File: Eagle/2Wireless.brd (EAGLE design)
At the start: 62.7 x 31.8 mm, 22 parts, among them IC1 TCA9517A, IC2 VREGLD1117, IC3 MB85RS2MTAPNF-G-BDERE1, U1 PHOTON_WITH_HEADERS

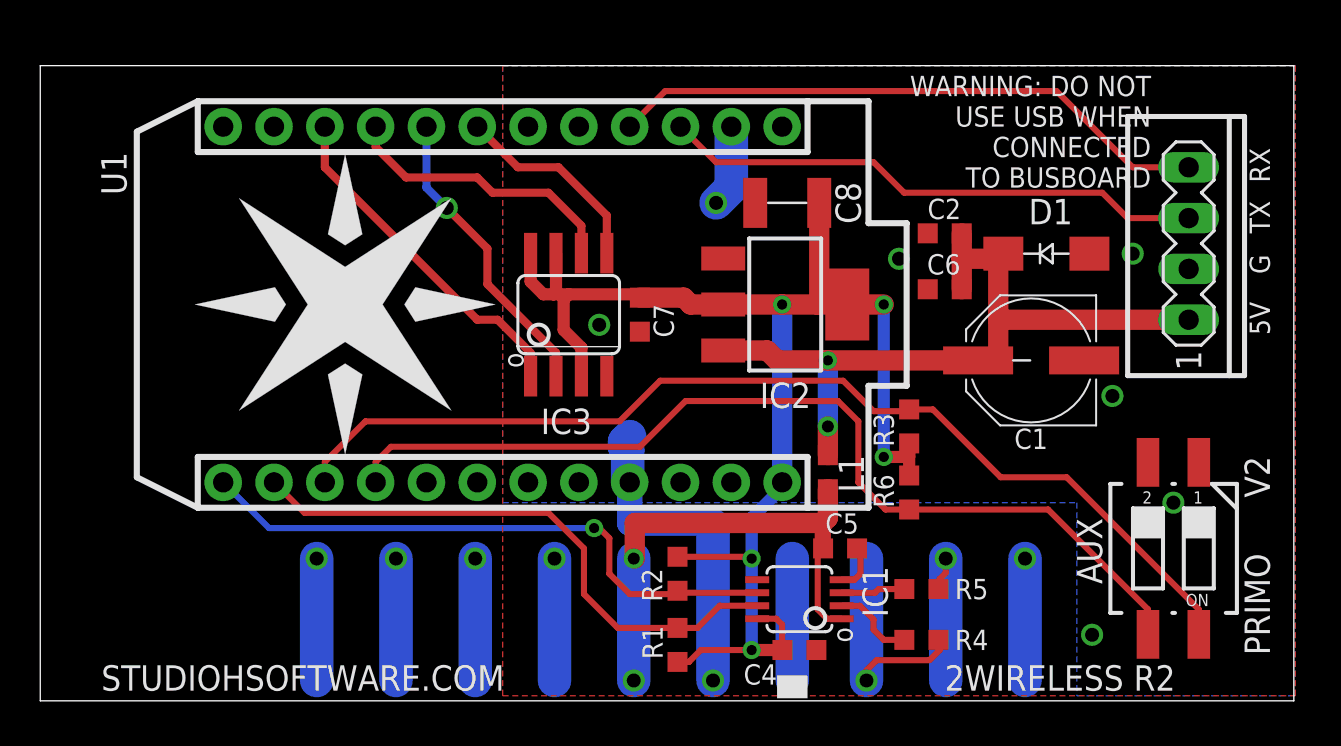
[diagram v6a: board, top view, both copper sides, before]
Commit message: Switch layout from Photon to Arduino MKR1000.
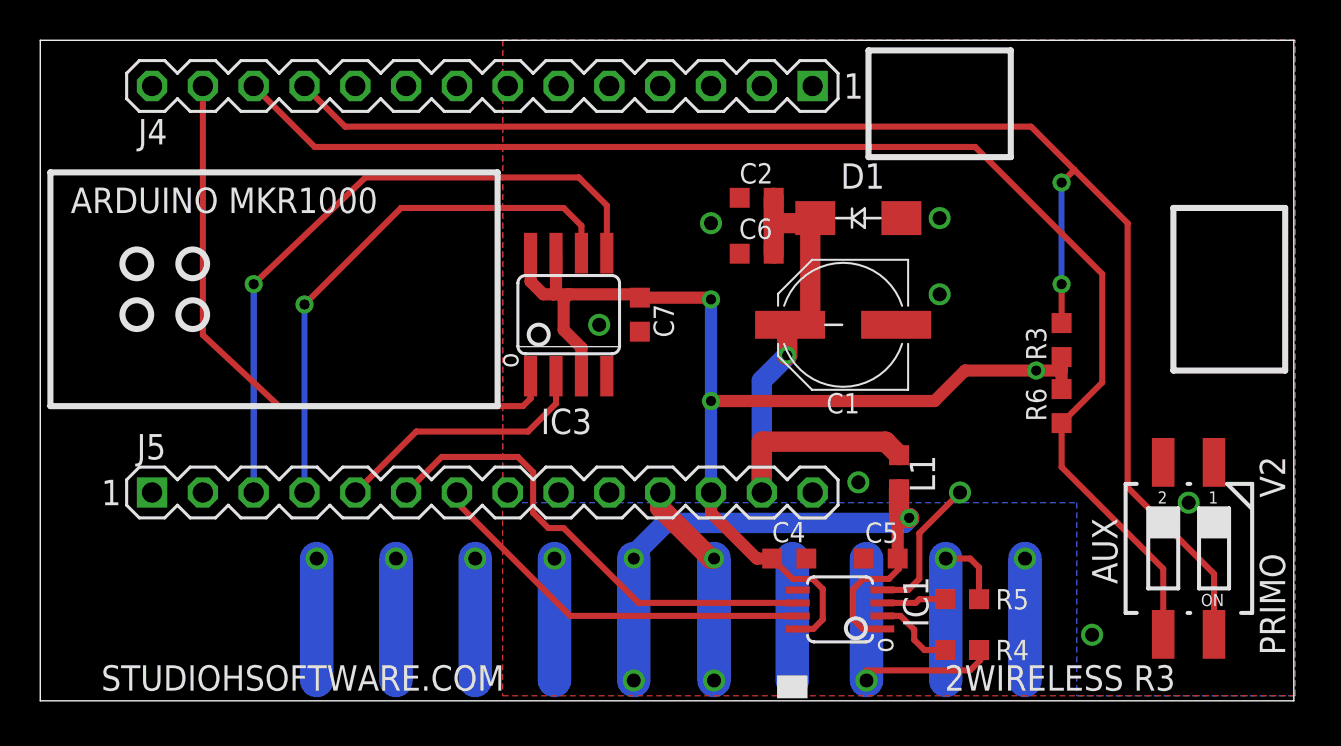
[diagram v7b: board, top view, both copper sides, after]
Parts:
- removed C8: 10u, studio_h:C1210
- removed IC2: VREGLD1117, studio_h:SOT223
- removed R1, R2: 2k, studio_h:R0603
- removed SV1: (no value), studio_h:MA04-1
- removed U$1: (no value), Particle:PARTICLE_LOGO_15MM
- removed U1: PHOTON_WITH_HEADERS, Particle:PHOTON
- added J4, J5: (no value), studio_h:MA14-1
- moved C1 9.56 mm to (40.1, 18.8)
- moved C2 9.56 mm to (35.8, 25.1)
- moved C6 9.56 mm to (35.8, 22.4)
- moved D1 9.56 mm to (40.9, 24.1)
- moved R3 8.76 mm to (51.1, 18.0)
- moved R6 8.76 mm to (51.1, 14.7)
- moved C4 4.60 mm to (37.4, 7.11)
- moved L1 3.56 mm to (42.9, 11.4)
- moved C5 2.09 mm to (42.0, 7.11), turned to 180 degrees
- moved R4 2.09 mm to (46.1, 2.54)
- moved R5 2.09 mm to (46.1, 5.08)
- moved IC1 2.09 mm to (40.0, 4.57)
- moved S1 0.76 mm to (57.4, 7.62)
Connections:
- removed net RX: SV1.4, U1.4
- removed net TX: SV1.3, U1.3
- removed net VBAT: U1.22
- removed net VIN: U1.1
- net !CS: now also J4.13; no longer U1.10
- net +5V: now also J5.13; no longer IC2.3, SV1.1
- net DGND: now also J5.11; no longer C8.2, IC2.1, SV1.2, U1.2, U1.21
- net DI-AUX: now also J4.12; no longer U1.16
- net DI-VERSION: now also J4.11; no longer U1.15
- net DPWR: now also J5.12; no longer C8.1, IC2.2, IC2.4, R1.2, R2.2, U1.24
- net MISO: now also J5.5; no longer U1.8
- net MOSI: now also J5.3; no longer U1.7
- net SCK: now also J5.4; no longer U1.9
- net SCL: now also J5.7; no longer R1.1, U1.14
- net SDA: now also J5.6; no longer R2.1, U1.13
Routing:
- net RX: track 30.3 -> 0.00 mm
- net TX: track 27.3 -> 0.00 mm
- net MOSI: track 10.2 -> 33.2 mm, vias 0 -> 1
- net DI-VERSION: track 52.4 -> 74.3 mm, vias 0 -> 2
- net DI-AUX: track 48.9 -> 67.3 mm
- net !CS: track 17.3 -> 31.5 mm
- net DPWR: track 72.4 -> 59.4 mm, vias 5 -> 3
- net SCK: track 14.3 -> 27.0 mm, vias 0 -> 1
- net SCL: track 29.0 -> 19.9 mm
- net +5V: track 38.0 -> 29.4 mm, vias 2 -> 1
- net EDAC-5V+: track 25.4 -> 31.7 mm, vias 2 -> 3
- net SDA: track 30.2 -> 24.5 mm, vias 1 -> 0
- net DGND: track 23.0 -> 18.6 mm, vias 8 -> 10
- net MISO: track 15.2 -> 13.2 mm, vias 1 -> 0
- net EDAC-I2C-CLK: track 11.2 -> 13.0 mm
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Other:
- board size 62.7 x 31.8 mm -> 62.7 x 33 mm
- board text added: "2WIRELESS R3"
- board text added: "ARDUINO MKR1000"
- board text removed: "2WIRELESS R2"
- board text removed: "5V"
- board text removed: "G"
- board text removed: "RX"
- board text removed: "TX"
- board text removed: "WARNING: DO NOT USE USB WHEN CONNECTED TO BUSBOARD"

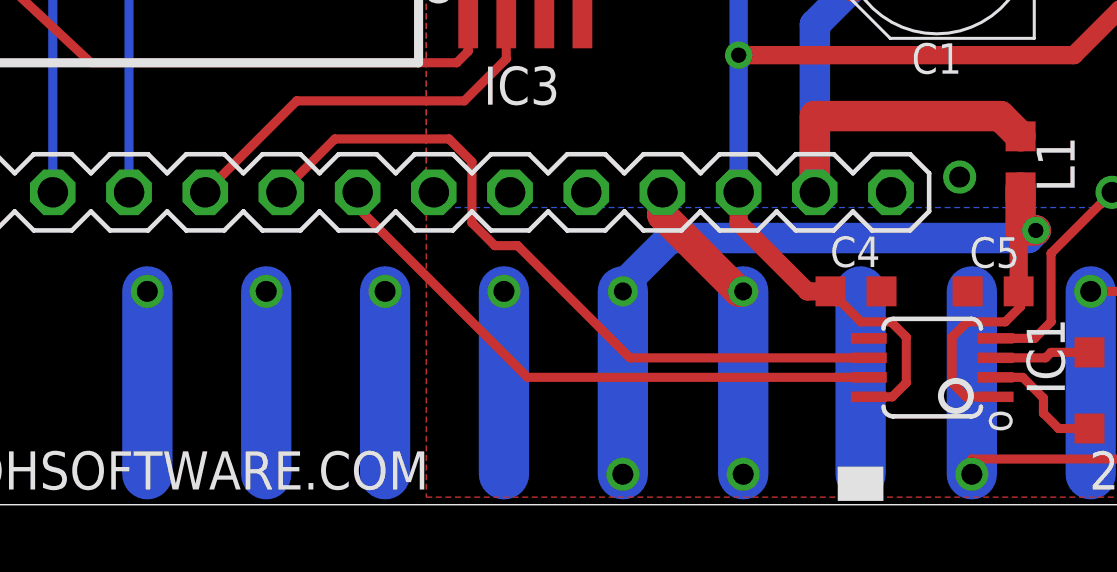
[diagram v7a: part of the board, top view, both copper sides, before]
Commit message: Add I2C pullups to MKR1000 layout.
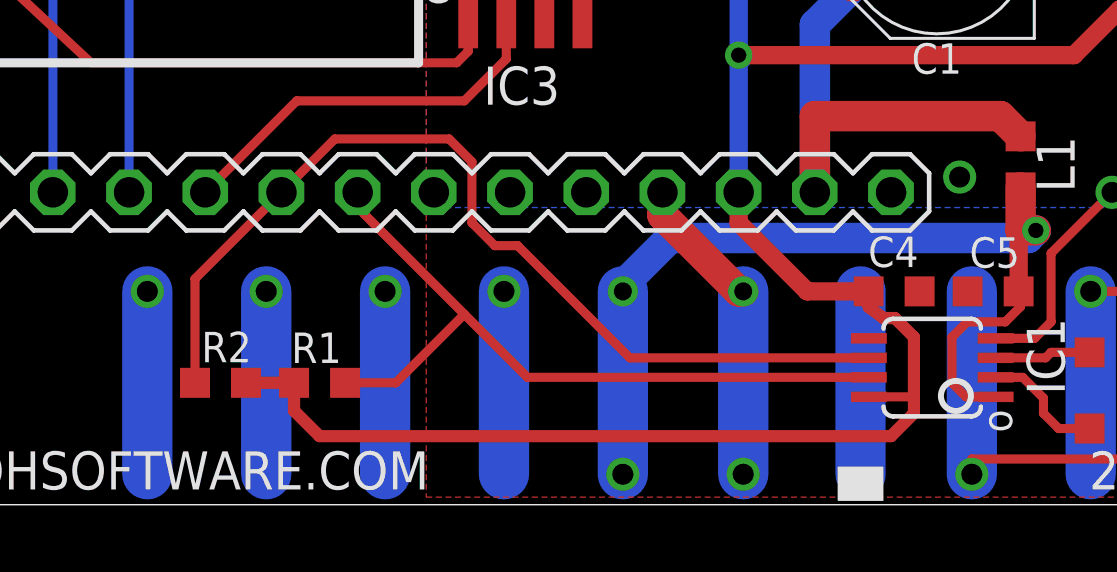
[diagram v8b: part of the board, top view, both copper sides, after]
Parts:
- added R1, R2: 2k, studio_h:R0603
- moved C4 1.27 mm to (38.7, 7.11)
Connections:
- net DPWR: now also R1.2, R2.2
- net SCL: now also R1.1
- net SDA: now also R2.1
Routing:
- net DPWR: track 59.4 -> 84.9 mm
- net SDA: track 24.5 -> 32.1 mm
- net SCL: track 19.9 -> 24.8 mm
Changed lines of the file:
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@@
 <attribute name="VALUE" x="27.992" y="19.939" size="1.016" layer="27" font="vector" ratio="12" rot="R270"/>
 </element>
-<element name="C4" library="studio_h" package="C0603" value="100n" x="37.4396" y="7.112" smashed="yes">
-<attribute name="NAME" x="36.576" y="7.924" size="1.016" layer="25" font="vector" ratio="12"/>
-<attribute name="Z_SMT" value="Y" x="37.4396" y="7.112" size="1.778" layer="27" display="off"/>
+<element name="C4" library="studio_h" package="C0603" value="100n" x="38.7096" y="7.112" smashed="yes">
+<attribute name="NAME" x="37.846" y="7.924" size="1.016" layer="25" font="vector" ratio="12"/>
+<attribute name="Z_SMT" value="Y" x="38.7096" y="7.112" size="1.778" layer="27" display="off"/>
 </element>
 <element name="R4" library="studio_h" package="R0603" value="30" x="46.0756" y="2.54" smashed="yes">
@@
 <attribute name="VALUE" x="4.318" y="7.493" size="1.27" layer="27" ratio="10"/>
 </element>
+<element name="R1" library="studio_h" package="R0603" value="2k" x="19.558" y="4.064" smashed="yes" rot="R180">
+<attribute name="Z_SMT" value="Y" x="19.558" y="4.064" size="1.778" layer="27" rot="R180" display="off"/>
+<attribute name="NAME" x="18.6182" y="4.7252" size="1.016" layer="25" font="vector" ratio="12"/>
+<attribute name="VALUE" x="20.193" y="6.044" size="1.016" layer="27" font="vector" ratio="12" rot="R180"/>
+</element>
+<element name="R2" library="studio_h" package="R0603" value="2k" x="16.256" y="4.064" smashed="yes">
+<attribute name="Z_SMT" value="Y" x="16.256" y="4.064" size="1.778" layer="27" display="off"/>
+<attribute name="NAME" x="15.621" y="4.749" size="1.016" layer="25" font="vector" ratio="12"/>
+<attribute name="VALUE" x="15.621" y="2.084" size="1.016" layer="27" font="vector" ratio="12"/>
+</element>
 </elements>
 <signals>
@@
 <contactref element="J5" pad="7"/>
 <wire x1="37.8676" y1="4.246" x2="26.488" y2="4.246" width="0.3048" layer="1"/>
-<wire x1="26.488" y1="4.246" x2="20.828" y2="9.906" width="0.3048" layer="1"/>
+<wire x1="26.488" y1="4.246" x2="24.384" y2="6.35" width="0.3048" layer="1"/>
+<wire x1="24.384" y1="6.35" x2="20.828" y2="9.906" width="0.3048" layer="1"/>
 <wire x1="20.828" y1="10.414" x2="20.828" y2="9.906" width="0.3048" layer="1"/>
+<contactref element="R1" pad="1"/>
+<wire x1="20.408" y1="4.064" x2="22.098" y2="4.064" width="0.3048" layer="1"/>
+<wire x1="22.098" y1="4.064" x2="24.384" y2="6.35" width="0.3048" layer="1"/>
 </signal>
 <signal name="SDA">
@@
 <wire x1="24.638" y1="9.398" x2="25.4" y2="8.636" width="0.3048" layer="1"/>
 <wire x1="25.4" y1="8.636" x2="26.162" y2="8.636" width="0.3048" layer="1"/>
+<contactref element="R2" pad="1"/>
+<wire x1="15.406" y1="4.064" x2="15.406" y2="7.532" width="0.3048" layer="1"/>
+<wire x1="15.406" y1="7.532" x2="18.288" y2="10.414" width="0.3048" layer="1"/>
 </signal>
 <signal name="EDAC-15V-" class="1">
@@
 <wire x1="33.528" y1="14.986" x2="33.782" y2="14.986" width="0.6096" layer="16"/>
 <wire x1="33.782" y1="14.986" x2="33.528" y2="14.732" width="0.6096" layer="16"/>
-<wire x1="36.5896" y1="7.112" x2="35.814" y2="7.112" width="0.6096" layer="1"/>
+<wire x1="37.8596" y1="7.112" x2="35.814" y2="7.112" width="0.6096" layer="1"/>
 <wire x1="35.814" y1="7.112" x2="33.528" y2="9.398" width="0.6096" layer="1"/>
 <wire x1="33.528" y1="9.398" x2="33.528" y2="10.414" width="0.6096" layer="1"/>
-<wire x1="37.8676" y1="3.596" x2="38.648" y2="3.596" width="0.3048" layer="1"/>
-<wire x1="38.648" y1="3.596" x2="39.116" y2="4.064" width="0.3048" layer="1"/>
-<wire x1="39.116" y1="4.064" x2="39.116" y2="5.588" width="0.3048" layer="1"/>
-<wire x1="39.116" y1="5.588" x2="38.608" y2="6.096" width="0.3048" layer="1"/>
-<wire x1="38.608" y1="6.096" x2="37.6056" y2="6.096" width="0.3048" layer="1"/>
-<wire x1="37.6056" y1="6.096" x2="36.5896" y2="7.112" width="0.3048" layer="1"/>
+<contactref element="R2" pad="2"/>
+<contactref element="R1" pad="2"/>
+<wire x1="37.8596" y1="7.112" x2="37.8596" y2="6.5904" width="0.4064" layer="1"/>
+<wire x1="37.8596" y1="6.5904" x2="38.354" y2="6.223" width="0.4064" layer="1"/>
+<wire x1="38.354" y1="6.223" x2="38.735" y2="6.223" width="0.4064" layer="1"/>
+<wire x1="38.735" y1="6.223" x2="39.37" y2="5.588" width="0.4064" layer="1"/>
+<wire x1="39.37" y1="5.588" x2="39.37" y2="3.556" width="0.4064" layer="1"/>
+<wire x1="39.37" y1="3.556" x2="39.37" y2="3.048" width="0.4064" layer="1"/>
+<wire x1="39.37" y1="3.048" x2="38.608" y2="2.286" width="0.4064" layer="1"/>
+<wire x1="38.608" y1="2.286" x2="19.558" y2="2.286" width="0.4064" layer="1"/>
+<wire x1="19.558" y1="2.286" x2="18.708" y2="3.136" width="0.4064" layer="1"/>
+<wire x1="17.106" y1="4.064" x2="18.708" y2="4.064" width="0.4064" layer="1"/>
+<wire x1="18.708" y1="4.064" x2="18.708" y2="3.136" width="0.4064" layer="1"/>
+<wire x1="37.8676" y1="3.596" x2="39.33" y2="3.596" width="0.3048" layer="1"/>
+<wire x1="39.33" y1="3.596" x2="39.37" y2="3.556" width="0.3048" layer="1"/>
 </signal>
 <signal name="DI-VERSION">
